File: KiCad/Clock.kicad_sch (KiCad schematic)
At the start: 25 parts, among them J1 USB_C_Receptacle_USB2.0, J2 SWD, J3 DISP, J4 BASE, Q1 PMV75UP, Q2 PMV75UP, Q3 PMV65UN, U1 Pico, U2 LM4040C30, U3 Keystone 2xAA 1012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

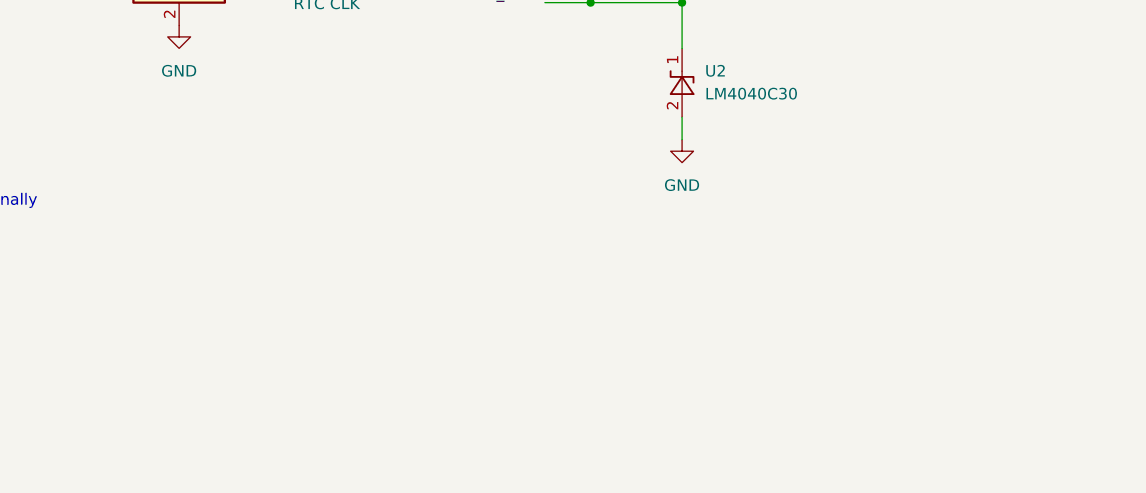
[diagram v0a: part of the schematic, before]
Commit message: Adjust the PCB for fabrication
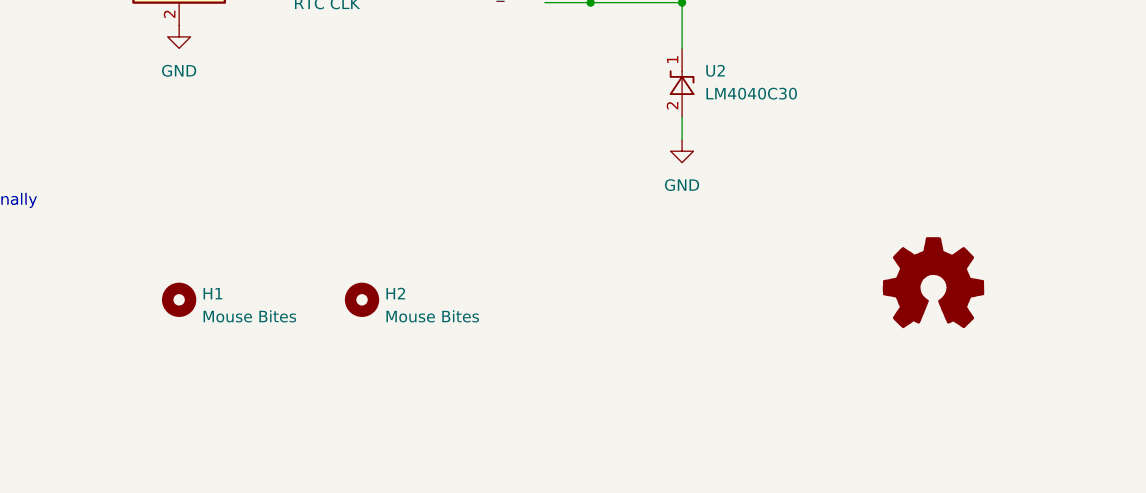
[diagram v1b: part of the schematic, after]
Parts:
- added H1, H2: Mouse Bites, Custom:MouseBites_2x05mm, symbol Mechanical:MountingHole
- added SYM1: Logo_Open_Hardware_Small, Symbol:OSHW-Logo2_24.3x20mm_SilkScreen, symbol Graphic:Logo_Open_Hardware_Small
- U1: footprint RPi_Pico:RPi_Pico_SMD_TH -> RPi_Pico:RPi_Pico_SMD
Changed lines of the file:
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@@
       (effects (font (size 1.27 1.27)) (justify left))
     )
-    (property "Footprint" "RPi_Pico:RPi_Pico_SMD_TH" (at 43.18 74.93 90)
+    (property "Footprint" "RPi_Pico:RPi_Pico_SMD" (at 43.18 74.93 90)
       (effects (font (size 1.27 1.27)) hide)
     )
@@
     )
   )
+  (symbol (lib_id "Mechanical:MountingHole") (at 101.6 175.26 0) (unit 1)
+    (in_bom yes) (on_board yes) (dnp no) (fields_autoplaced)
+    (property "Reference" "H1" (at 104.14 174.625 0)
+      (effects (font (size 1.27 1.27)) (justify left))
+    )
+    (property "Value" "Mouse Bites" (at 104.14 177.165 0)
+      (effects (font (size 1.27 1.27)) (justify left))
+    )
+    (property "Footprint" "Custom:MouseBites_2x05mm" (at 101.6 175.26 0)
+      (effects (font (size 1.27 1.27)) hide)
+    )
+    (property "Datasheet" "~" (at 101.6 175.26 0)
+      (effects (font (size 1.27 1.27)) hide)
+    )
+    (instances
+      (project "Clock"
+        (path "/f7699a6c-47c6-4861-bf17-120f6a38a8b0"
+          (reference "H1") (unit 1)
+        )
+      )
+    )
+  )
   (symbol (lib_id "Connector:TestPoint") (at 111.76 137.16 180) (unit 1)
     (in_bom yes) (on_board yes) (dnp no) (fields_autoplaced)
@@
         (path "/f7699a6c-47c6-4861-bf17-120f6a38a8b0"
           (reference "R2") (unit 1)
+        )
+      )
+    )
+  )
+  (symbol (lib_id "Mechanical:MountingHole") (at 121.92 175.26 0) (unit 1)
+    (in_bom yes) (on_board yes) (dnp no) (fields_autoplaced)
+    (property "Reference" "H2" (at 124.46 174.625 0)
+      (effects (font (size 1.27 1.27)) (justify left))
+    )
+    (property "Value" "Mouse Bites" (at 124.46 177.165 0)
+      (effects (font (size 1.27 1.27)) (justify left))
+    )
+    (property "Footprint" "Custom:MouseBites_2x05mm" (at 121.92 175.26 0)
+      (effects (font (size 1.27 1.27)) hide)
+    )
+    (property "Datasheet" "~" (at 121.92 175.26 0)
+      (effects (font (size 1.27 1.27)) hide)
+    )
+    (instances
+      (project "Clock"
+        (path "/f7699a6c-47c6-4861-bf17-120f6a38a8b0"
+          (reference "H2") (unit 1)
         )
       )
@@
         )
       )
+    )
+  )
+  (symbol (lib_id "Graphic:Logo_Open_Hardware_Small") (at 185.42 173.99 0) (unit 1)
+    (in_bom no) (on_board yes) (dnp no) (fields_autoplaced)
+    (property "Reference" "SYM1" (at 185.42 167.005 0)
+      (effects (font (size 1.27 1.27)) hide)
+    )
+    (property "Value" "Logo_Open_Hardware_Small" (at 185.42 179.705 0)
+      (effects (font (size 1.27 1.27)) hide)
+    )
+    (property "Footprint" "Symbol:OSHW-Logo2_24.3x20mm_SilkScreen" (at 185.42 173.99 0)
+      (effects (font (size 1.27 1.27)) hide)
+    )
+    (property "Datasheet" "~" (at 185.42 173.99 0)
+      (effects (font (size 1.27 1.27)) hide)
+    )
+    (property "Sim.Enable" "0" (at 185.42 173.99 0)
+      (effects (font (size 1.27 1.27)) hide)
+    )
+    (instances
+      (project "Clock"
+        (path "/f7699a6c-47c6-4861-bf17-120f6a38a8b0"
+          (reference "SYM1") (unit 1)
+        )
+      )

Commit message: Attach the 3D model of Pico (again), update TODOs, update ".gitignore"
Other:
- note added: "Nexperia MOSFETs P-ch. PMV75UP N-ch. PMV65UN"
- note added: "TODO: - Add TVS diodes to the sensor buttons? - Consider adding test-points for power consumption profiling, etc."
- note removed: "Nexperia MOSFETs P-ch. PMV75UP, NXV75UP N-ch. PMV65UN, NXV65UN"
- note removed: "TODO: - Add sensor buttons (with TVS diodes?) - Add the battery holder footprint - Consider adding test-points for power consumption profiling, etc."
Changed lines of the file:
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@@
     (effects (font (size 1.27 1.27)) (justify left bottom))
   )
-  (text "Nexperia MOSFETs\nP-ch. PMV75UP, NXV75UP\nN-ch. PMV65UN, NXV65UN"
-    (at 129.54 21.59 0)
+  (text "Nexperia MOSFETs\nP-ch. PMV75UP\nN-ch. PMV65UN" (at 129.54 21.59 0)
     (effects (font (size 1.27 1.27)) (justify left bottom))
   )
@@
     (effects (font (size 1.27 1.27)) (justify left bottom))
   )
-  (text "TODO:\n- Add sensor buttons (with TVS diodes?)\n- Add the battery holder footprint\n- Consider adding test-points for power consumption profiling, etc."
+  (text "TODO:\n- Add TVS diodes to the sensor buttons?\n- Consider adding test-points for power consumption profiling, etc."
     (at 27.94 25.4 0)
     (effects (font (size 1.27 1.27)) (justify left bottom))

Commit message: Update the charge-discharge current limiting resistors from 4.7R to 5.6R (what I had in stock when assembling the boards)
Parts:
- R8, R9: value 4.7 0.5W -> 5.6 0.5W
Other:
- note added: "NOTE: There must be a bypass-capacitor!"
- note added: "TODO: Optimize the SM footprint."
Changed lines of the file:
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@@
     (stroke (width 0) (type default))
+  )
+  (text "NOTE: There must be a bypass-capacitor!" (at 83.82 146.05 0)
+    (effects (font (size 1.27 1.27)) (justify left bottom))
   )
   (text "2S AA NiMH 2.5 Ah\n(Eneloop Pro BK-3HCD(E))" (at 246.38 60.96 0)
@@
   (text "RP2040 pins are reset to\ninput w/ pull-down 50–80 kOhm."
     (at 121.92 85.09 0)
+    (effects (font (size 1.27 1.27)) (justify left bottom))
+  )
+  (text "TODO: Optimize the SM footprint." (at 49.53 110.49 0)
     (effects (font (size 1.27 1.27)) (justify left bottom))
   )
@@
       (effects (font (size 1.27 1.27)))
     )
-    (property "Value" "4.7 0.5W" (at 194.31 46.99 90)
+    (property "Value" "5.6 0.5W" (at 194.31 46.99 90)
       (effects (font (size 1.27 1.27)))
     )
@@
       (effects (font (size 1.27 1.27)))
     )
-    (property "Value" "4.7 0.5W" (at 194.31 57.15 90)
-      (effects (font (size 1.27 1.27)))
-    )
+    (property "Value" "5.6 0.5W" (at 194.31 57.15 90)
+      (effects (font (size 1.27 1.27)))
+    )
